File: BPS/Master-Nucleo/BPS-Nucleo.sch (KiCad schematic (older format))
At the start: 14 parts, among them J12 Conn_01x04, U1 NUCLEO144-F412ZG

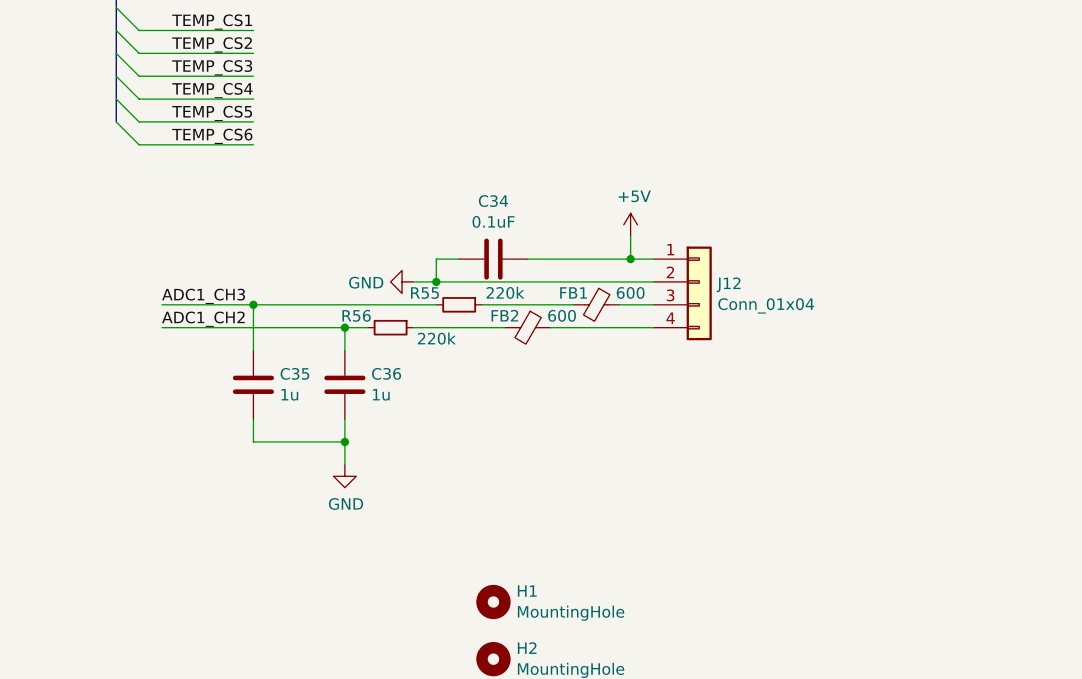
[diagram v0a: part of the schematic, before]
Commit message: worked on pcb layout and schematic
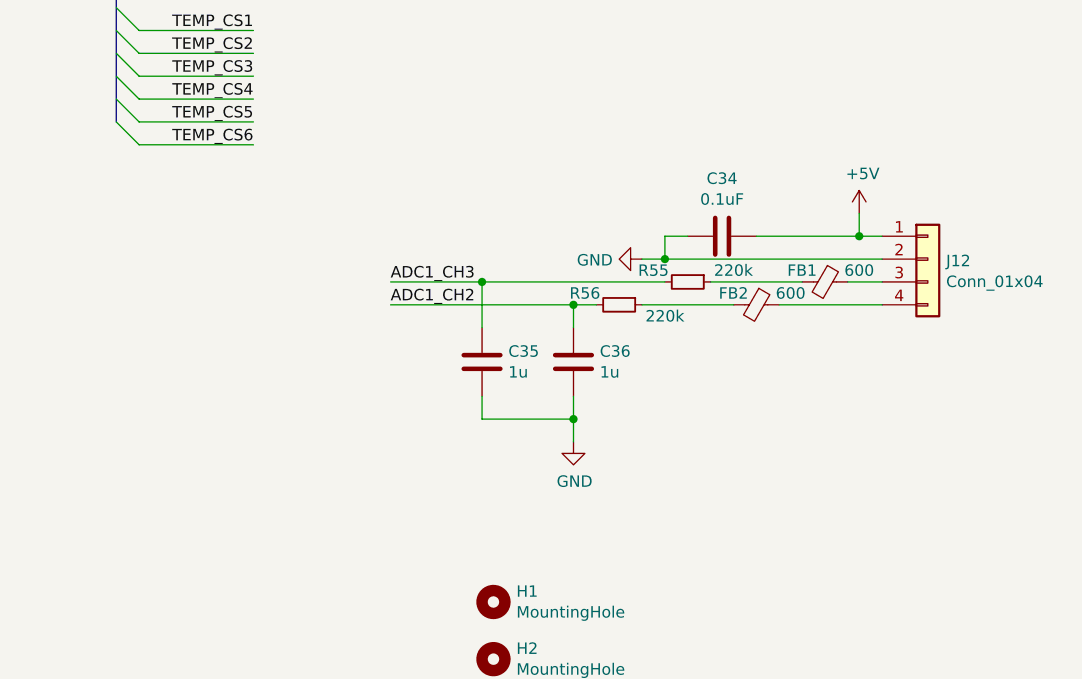
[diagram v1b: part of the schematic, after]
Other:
- moved on the sheet: C34, C35, C36, FB1, FB2, J12, R55, R56
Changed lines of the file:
@@
 EESchema Schematic File Version 4
-EELAYER 29 0
+LIBS:BPS-Nucleo-cache
+EELAYER 26 0
 EELAYER END
 $Descr A3 16535 11693
@@
 L Connector_Generic:Conn_01x04 J12
 U 1 1 5D4B82ED
-P 13550 4450
-F 0 "J12" H 13630 4442 50  0000 L CNN
-F 1 "Conn_01x04" H 13630 4351 50  0000 L CNN
-F 2 "UTSVT_Connectors:Molex_MicroFit3.0_1x4xP3.00mm_PolarizingPeg_Vertical" H 13550 4450 50  0001 C CNN
-F 3 "~" H 13550 4450 50  0001 C CNN
-	1    13550 4450
+P 14550 4350
+F 0 "J12" H 14630 4342 50  0000 L CNN
+F 1 "Conn_01x04" H 14630 4251 50  0000 L CNN
+F 2 "UTSVT_Connectors:Molex_MicroFit3.0_1x4xP3.00mm_PolarizingPeg_Vertical" H 14550 4350 50  0001 C CNN
+F 3 "~" H 14550 4350 50  0001 C CNN
+	1    14550 4350
 	1    0    0    -1
 $EndComp
@@
 L Device:C C34
 U 1 1 5D4BE51F
-P 12650 4350
-F 0 "C34" V 12398 4350 50  0000 C CNN
-F 1 "0.1uF" V 12489 4350 50  0000 C CNN
-F 2 "Capacitor_SMD:C_0805_2012Metric" H 12688 4200 50  0001 C CNN
-F 3 "~" H 12650 4350 50  0001 C CNN
-	1    12650 4350
+P 13650 4250
+F 0 "C34" V 13398 4250 50  0000 C CNN
+F 1 "0.1uF" V 13489 4250 50  0000 C CNN
+F 2 "Capacitor_SMD:C_0805_2012Metric" H 13688 4100 50  0001 C CNN
+F 3 "~" H 13650 4250 50  0001 C CNN
+	1    13650 4250
 	0    1    1    0
 $EndComp
@@
 L power:+5V #PWR0197
 U 1 1 5D4BF120
-P 13250 4250
-F 0 "#PWR0197" H 13250 4100 50  0001 C CNN
-F 1 "+5V" H 13265 4423 50  0000 C CNN
-F 2 "" H 13250 4250 50  0001 C CNN
-F 3 "" H 13250 4250 50  0001 C CNN
-	1    13250 4250
+P 14250 4150
+F 0 "#PWR0197" H 14250 4000 50  0001 C CNN
+F 1 "+5V" H 14265 4323 50  0000 C CNN
+F 2 "" H 14250 4150 50  0001 C CNN
+F 3 "" H 14250 4150 50  0001 C CNN
+	1    14250 4150
 	1    0    0    -1
 $EndComp
@@
 L Device:Ferrite_Bead_Small FB1
 U 1 1 5D4C1892
-P 13100 4550
-F 0 "FB1" V 13050 4450 50  0000 C CNN
-F 1 "600" V 13050 4700 50  0000 C CNN
-F 2 "Inductor_SMD:L_0805_2012Metric" V 13030 4550 50  0001 C CNN
-F 3 "~" H 13100 4550 50  0001 C CNN
-	1    13100 4550
+P 14100 4450
+F 0 "FB1" V 14050 4350 50  0000 C CNN
+F 1 "600" V 14050 4600 50  0000 C CNN
+F 2 "Inductor_SMD:L_0805_2012Metric" V 14030 4450 50  0001 C CNN
+F 3 "~" H 14100 4450 50  0001 C CNN
+	1    14100 4450
 	0    1    1    0
 $EndComp
@@
 L Device:Ferrite_Bead_Small FB2
 U 1 1 5D4C1FFC
-P 12800 4650
-F 0 "FB2" V 12750 4550 50  0000 C CNN
-F 1 "600" V 12750 4800 50  0000 C CNN
-F 2 "Inductor_SMD:L_0805_2012Metric" V 12730 4650 50  0001 C CNN
-F 3 "~" H 12800 4650 50  0001 C CNN
-	1    12800 4650
+P 13800 4550
+F 0 "FB2" V 13750 4450 50  0000 C CNN
+F 1 "600" V 13750 4700 50  0000 C CNN
+F 2 "Inductor_SMD:L_0805_2012Metric" V 13730 4550 50  0001 C CNN
+F 3 "~" H 13800 4550 50  0001 C CNN
+	1    13800 4550
 	0    1    1    0
 $EndComp
 Wire Wire Line
-	12900 4650 13350 4650
-Wire Wire Line
-	13350 4550 13200 4550
-Wire Wire Line
-	13350 4350 13250 4350
-Wire Wire Line
-	13250 4250 13250 4350
-Connection ~ 13250 4350
-Wire Wire Line
-	12400 4450 12400 4350
-Wire Wire Line
-	12400 4350 12500 4350
-Wire Wire Line
-	12400 4450 12300 4450
-Connection ~ 12400 4450
+	13900 4550 14350 4550
+Wire Wire Line
+	14350 4450 14200 4450
+Wire Wire Line
+	14350 4250 14250 4250
+Wire Wire Line
+	14250 4150 14250 4250
+Connection ~ 14250 4250
+Wire Wire Line
+	13400 4350 13400 4250
+Wire Wire Line
+	13400 4250 13500 4250
+Wire Wire Line
+	13400 4350 13300 4350
+Connection ~ 13400 4350
 $Comp
 L power:GND #PWR0198
 U 1 1 5D4DE20B
-P 12300 4450
-F 0 "#PWR0198" H 12300 4200 50  0001 C CNN
-F 1 "GND" V 12305 4322 50  0000 R CNN
-F 2 "" H 12300 4450 50  0001 C CNN
-F 3 "" H 12300 4450 50  0001 C CNN
-	1    12300 4450
+P 13300 4350
+F 0 "#PWR0198" H 13300 4100 50  0001 C CNN
+F 1 "GND" V 13305 4222 50  0000 R CNN
+F 2 "" H 13300 4350 50  0001 C CNN
+F 3 "" H 13300 4350 50  0001 C CNN
+	1    13300 4350
 	0    1    1    0
 $EndComp
@@
 L Device:R_Small R56
 U 1 1 5D4DEF80
-P 12200 4650
-F 0 "R56" V 12150 4500 50  0000 C CNN
-F 1 "220k" V 12250 4850 50  0000 C CNN
-F 2 "Resistor_SMD:R_0805_2012Metric" H 12200 4650 50  0001 C CNN
-F 3 "~" H 12200 4650 50  0001 C CNN
-	1    12200 4650
+P 13200 4550
+F 0 "R56" V 13150 4400 50  0000 C CNN
+F 1 "220k" V 13250 4750 50  0000 C CNN
+F 2 "Resistor_SMD:R_0805_2012Metric" H 13200 4550 50  0001 C CNN
+F 3 "~" H 13200 4550 50  0001 C CNN
+	1    13200 4550
 	0    1    1    0
 $EndComp
@@
 L Device:R_Small R55
 U 1 1 5D4DF70C
-P 12500 4550
-F 0 "R55" V 12450 4400 50  0000 C CNN
-F 1 "220k" V 12450 4750 50  0000 C CNN
-F 2 "Resistor_SMD:R_0805_2012Metric" H 12500 4550 50  0001 C CNN
-F 3 "~" H 12500 4550 50  0001 C CNN
-	1    12500 4550
+P 13500 4450
+F 0 "R55" V 13450 4300 50  0000 C CNN
+F 1 "220k" V 13450 4650 50  0000 C CNN
+F 2 "Resistor_SMD:R_0805_2012Metric" H 13500 4450 50  0001 C CNN
+F 3 "~" H 13500 4450 50  0001 C CNN
+	1    13500 4450
 	0    1    1    0
 $EndComp
 Wire Wire Line
-	12300 4650 12700 4650
-Wire Wire Line
-	13000 4550 12600 4550
-Wire Wire Line
-	12800 4350 13250 4350
-Wire Wire Line
-	12400 4450 13350 4450
-Wire Wire Line
-	12100 4650 12000 4650
+	13300 4550 13700 4550
+Wire Wire Line
+	14000 4450 13600 4450
+Wire Wire Line
+	13800 4250 14250 4250
+Wire Wire Line
+	13400 4350 14350 4350
+Wire Wire Line
+	13100 4550 13000 4550
 $Comp
 L Device:C C36
 U 1 1 5D5097C7
-P 12000 4900
-F 0 "C36" H 11885 4854 50  0000 R CNN
-F 1 "1u" H 11885 4945 50  0000 R CNN
-F 2 "Capacitor_SMD:C_0805_2012Metric" H 12038 4750 50  0001 C CNN
-F 3 "~" H 12000 4900 50  0001 C CNN
-	1    12000 4900
+P 13000 4800
+F 0 "C36" H 12885 4754 50  0000 R CNN
+F 1 "1u" H 12885 4845 50  0000 R CNN
+F 2 "Capacitor_SMD:C_0805_2012Metric" H 13038 4650 50  0001 C CNN
+F 3 "~" H 13000 4800 50  0001 C CNN
+	1    13000 4800
 	-1   0    0    1
 $EndComp
@@
 L Device:C C35
 U 1 1 5D50A78C
-P 11600 4900
-F 0 "C35" H 11485 4854 50  0000 R CNN
-F 1 "1u" H 11485 4945 50  0000 R CNN
-F 2 "Capacitor_SMD:C_0805_2012Metric" H 11638 4750 50  0001 C CNN
-F 3 "~" H 11600 4900 50  0001 C CNN
-	1    11600 4900
+P 12600 4800
+F 0 "C35" H 12485 4754 50  0000 R CNN
+F 1 "1u" H 12485 4845 50  0000 R CNN
+F 2 "Capacitor_SMD:C_0805_2012Metric" H 12638 4650 50  0001 C CNN
+F 3 "~" H 12600 4800 50  0001 C CNN
+	1    12600 4800
 	-1   0    0    1
 $EndComp
 Wire Wire Line
-	12000 4750 12000 4650
-Connection ~ 12000 4650
-Wire Wire Line
-	11600 4750 11600 4550
-Wire Wire Line
-	11600 4550 12400 4550
-Wire Wire Line
-	11200 4650 12000 4650
-Wire Wire Line
-	11600 4550 11200 4550
-Connection ~ 11600 4550
-Wire Wire Line
-	11600 5050 11600 5150
-Wire Wire Line
-	11600 5150 12000 5150
-Wire Wire Line
-	12000 5150 12000 5050
+	13000 4650 13000 4550
+Connection ~ 13000 4550
+Wire Wire Line
+	12600 4650 12600 4450
+Wire Wire Line
+	12600 4450 13400 4450
+Wire Wire Line
+	12200 4550 13000 4550
+Wire Wire Line
+	12600 4450 12200 4450
+Connection ~ 12600 4450
+Wire Wire Line
+	12600 4950 12600 5050
+Wire Wire Line
+	12600 5050 13000 5050
+Wire Wire Line
+	13000 5050 13000 4950
 $Comp
 L power:GND #PWR0199
 U 1 1 5D5271D2
-P 12000 5250
-F 0 "#PWR0199" H 12000 5000 50  0001 C CNN
-F 1 "GND" H 12005 5077 50  0000 C CNN
-F 2 "" H 12000 5250 50  0001 C CNN
-F 3 "" H 12000 5250 50  0001 C CNN
-	1    12000 5250
-	1    0    0    -1
-$EndComp
-Wire Wire Line
-	12000 5250 12000 5150
-Connection ~ 12000 5150
-Text Label 11200 4650 0    50   ~ 0
+P 13000 5150
+F 0 "#PWR0199" H 13000 4900 50  0001 C CNN
+F 1 "GND" H 13005 4977 50  0000 C CNN
+F 2 "" H 13000 5150 50  0001 C CNN
+F 3 "" H 13000 5150 50  0001 C CNN
+	1    13000 5150
+	1    0    0    -1
+$EndComp
+Wire Wire Line
+	13000 5150 13000 5050
+Connection ~ 13000 5050
+Text Label 12200 4550 0    50   ~ 0
 ADC1_CH2
-Text Label 11200 4550 0    50   ~ 0
+Text Label 12200 4450 0    50   ~ 0
 ADC1_CH3
-Wire Bus Line
-	11000 3150 11000 3750
 Wire Wire Line
 	11100 3850 11600 3850
@@
 Text Label 11000 3150 2    50   ~ 0
 TEMP_CS[1..6]
-Wire Bus Line
-	10100 2650 10100 2950
-Wire Bus Line
-	10100 5550 10100 6150
 Entry Wire Line
 	11000 3750 11100 3850
@@
 Text Label 11600 3850 2    50   ~ 0
 TEMP_CS6
+Wire Bus Line
+	10100 2650 10100 2950
+Wire Bus Line
+	10100 5550 10100 6150
+Wire Bus Line
+	11000 3150 11000 3750
 $EndSCHEMATC
